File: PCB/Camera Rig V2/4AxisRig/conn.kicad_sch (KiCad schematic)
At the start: 8 parts, among them J5 USB_C_Receptacle_USB2.0_14P

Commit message: PCB V2 first draft
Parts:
- removed J5: USB_C_Receptacle_USB2.0_14P, USB_C_Receptacle_USB2.0_14P:CONN_8p94X6p5X3p16_12L_GCC, symbol Connector:USB_C_Receptacle_USB2.0_14P
- added J5: USB_C_Receptacle_USB2.0_16P, USB_C_Receptacle_USB2.0_14P:CONN_8p94X6p5X3p16_12L_GCC, symbol Connector:USB_C_Receptacle_USB2.0_16P
- R36: renamed from R35; value 5.1k -> 5.1k+-10%
- R37: renamed from R36; value 5.1k -> 5.1k+-10%
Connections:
- net D+: now also J5.A6 (D+), J5.B6 (D+)
- net D-: now also J5.A7 (D-), J5.B7 (D-)
- net GND: now also J5.A1 (GND), J5.A12 (GND), J5.B1 (GND), J5.B12 (GND), J5.S1 (SHIELD)
- net VBUS: now also J5.A4 (VBUS), J5.A9 (VBUS), J5.B4 (VBUS), J5.B9 (VBUS)
- net CC1 renamed USB_CC1
- net USB_CC1: now also J5.A5 (CC1)
- net CC2 renamed USB_CC2
- net USB_CC2: now also J5.B5 (CC2)
- no-connect marks 0 -> 2
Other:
- moved on the sheet: R37

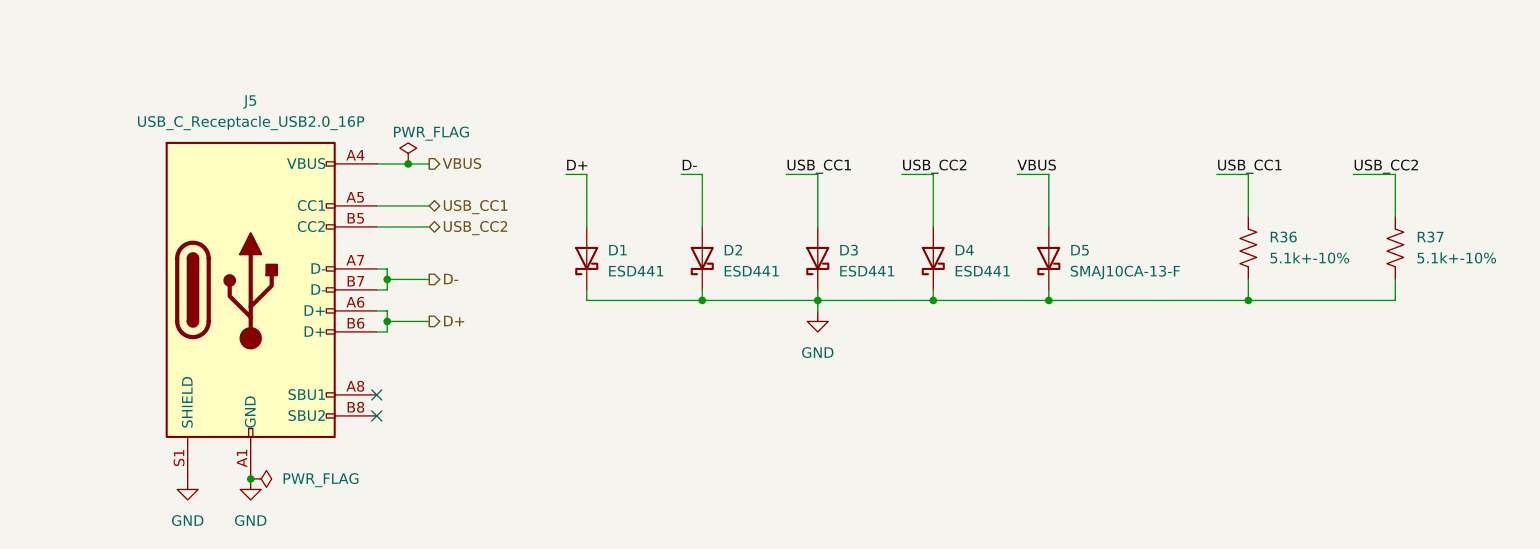
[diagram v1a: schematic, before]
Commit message: Netclass Improvements
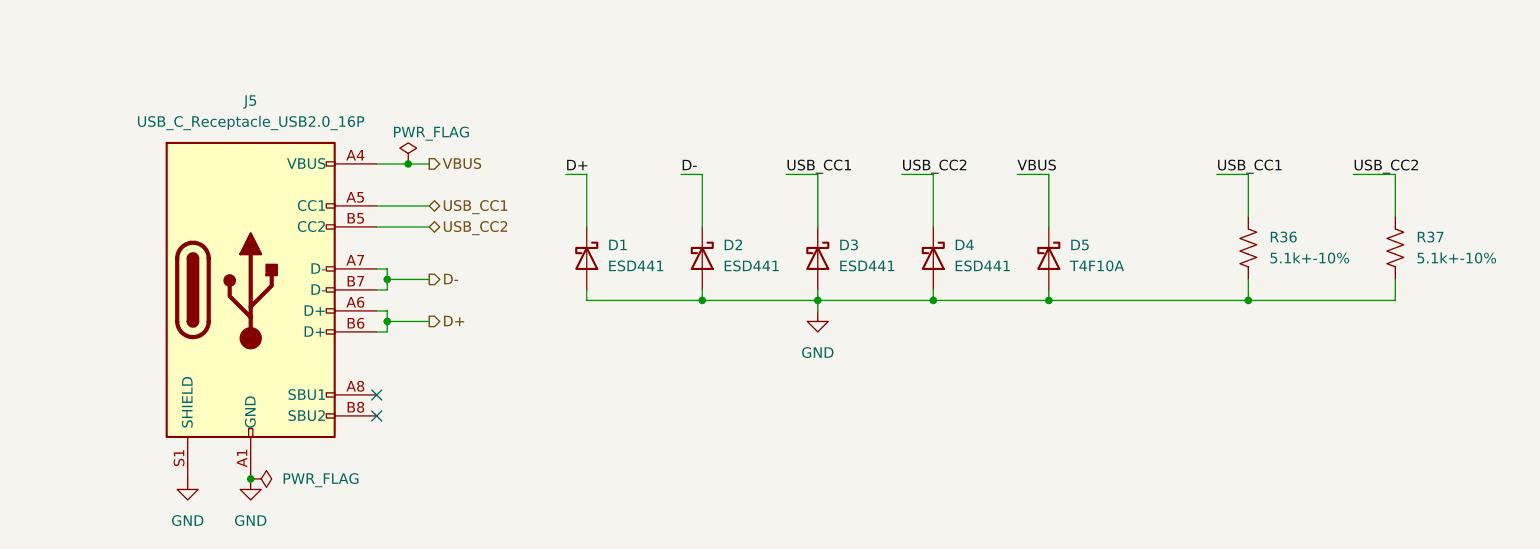
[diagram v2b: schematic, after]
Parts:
- D5: value SMAJ10CA-13-F -> T4F10A; footprint SMAJ10CA-13-F:SMA_DIO -> Diode_SMD:Nexperia_CFP3_SOD-123W
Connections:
- net D+: now also D1.1 (K); no longer D1.2 (A)
- net D-: now also D2.1 (K); no longer D2.2 (A)
- net GND: now also D1.2 (A), D2.2 (A), D3.2 (A), D4.2 (A), D5.2 (A); no longer D1.1 (K), D2.1 (K), D3.1 (K), D4.1 (K), D5.1 (K)
- net USB_CC1: now also D3.1 (K); no longer D3.2 (A)
- net USB_CC2: now also D4.1 (K); no longer D4.2 (A)
- net VBUS: now also D5.1 (K); no longer D5.2 (A)
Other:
- moved on the sheet: D1, D2, D3, D4, D5
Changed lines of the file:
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@@
 	(symbol
 		(lib_id "Device:D_Schottky")
-		(at 146.05 90.17 90)
+		(at 146.05 90.17 270)
 		(unit 1)
 		(exclude_from_sim no)
@@
 		(fields_autoplaced yes)
 		(property "Reference" "D2"
-			(at 148.59 89.2174 90)
-			(effects
-				(font
-					(size 1.27 1.27)
-				)
-				(justify right)
+			(at 148.59 88.5824 90)
+			(effects
+				(font
+					(size 1.27 1.27)
+				)
+				(justify left)
 			)
 		)
 		(property "Value" "ESD441"
-			(at 148.59 91.7574 90)
-			(effects
-				(font
-					(size 1.27 1.27)
-				)
-				(justify right)
+			(at 148.59 91.1224 90)
+			(effects
+				(font
+					(size 1.27 1.27)
+				)
+				(justify left)
 			)
 		)
@@
 	(symbol
 		(lib_id "Device:D_Schottky")
-		(at 173.99 90.17 90)
+		(at 173.99 90.17 270)
 		(unit 1)
 		(exclude_from_sim no)
@@
 		(fields_autoplaced yes)
 		(property "Reference" "D4"
-			(at 176.53 89.2174 90)
-			(effects
-				(font
-					(size 1.27 1.27)
-				)
-				(justify right)
+			(at 176.53 88.5824 90)
+			(effects
+				(font
+					(size 1.27 1.27)
+				)
+				(justify left)
 			)
 		)
 		(property "Value" "ESD441"
-			(at 176.53 91.7574 90)
-			(effects
-				(font
-					(size 1.27 1.27)
-				)
-				(justify right)
+			(at 176.53 91.1224 90)
+			(effects
+				(font
+					(size 1.27 1.27)
+				)
+				(justify left)
 			)
 		)
@@
 	(symbol
 		(lib_id "Device:D_Schottky")
-		(at 187.96 90.17 90)
+		(at 187.96 90.17 270)
 		(unit 1)
 		(exclude_from_sim no)
@@
 		(fields_autoplaced yes)
 		(property "Reference" "D5"
-			(at 190.5 89.2174 90)
-			(effects
-				(font
-					(size 1.27 1.27)
-				)
-				(justify right)
-			)
-		)
-		(property "Value" "SMAJ10CA-13-F"
-			(at 190.5 91.7574 90)
-			(effects
-				(font
-					(size 1.27 1.27)
-				)
-				(justify right)
-			)
-		)
-		(property "Footprint" "SMAJ10CA-13-F:SMA_DIO"
+			(at 190.5 88.5824 90)
+			(effects
+				(font
+					(size 1.27 1.27)
+				)
+				(justify left)
+			)
+		)
+		(property "Value" "T4F10A"
+			(at 190.5 91.1224 90)
+			(effects
+				(font
+					(size 1.27 1.27)
+				)
+				(justify left)
+			)
+		)
+		(property "Footprint" "Diode_SMD:Nexperia_CFP3_SOD-123W"
 			(at 187.96 90.17 0)
 			(effects
@@
 			)
 		)
-		(property "Datasheet" "https://www.diodes.com/assets/Datasheets/SMAJ5.0CA-SMAJ200CA.pdf"
+		(property "Datasheet" "DF2B7AFS"
 			(at 187.96 90.17 0)
 			(effects
@@
 	(symbol
 		(lib_id "Device:D_Schottky")
-		(at 160.02 90.17 90)
+		(at 160.02 90.17 270)
 		(unit 1)
 		(exclude_from_sim no)
@@
 		(fields_autoplaced yes)
 		(property "Reference" "D3"
-			(at 162.56 89.2174 90)
-			(effects
-				(font
-					(size 1.27 1.27)
-				)
-				(justify right)
+			(at 162.56 88.5824 90)
+			(effects
+				(font
+					(size 1.27 1.27)
+				)
+				(justify left)
 			)
 		)
 		(property "Value" "ESD441"
-			(at 162.56 91.7574 90)
-			(effects
-				(font
-					(size 1.27 1.27)
-				)
-				(justify right)
+			(at 162.56 91.1224 90)
+			(effects
+				(font
+					(size 1.27 1.27)
+				)
+				(justify left)
 			)
 		)
@@
 	(symbol
 		(lib_id "Device:D_Schottky")
-		(at 132.08 90.17 90)
+		(at 132.08 90.17 270)
 		(unit 1)
 		(exclude_from_sim no)
@@
 		(fields_autoplaced yes)
 		(property "Reference" "D1"
-			(at 134.62 89.2174 90)
-			(effects
-				(font
-					(size 1.27 1.27)
-				)
-				(justify right)
+			(at 134.62 88.5824 90)
+			(effects
+				(font
+					(size 1.27 1.27)
+				)
+				(justify left)
 			)
 		)
 		(property "Value" "ESD441"
-			(at 134.62 91.7574 90)
-			(effects
-				(font
-					(size 1.27 1.27)
-				)
-				(justify right)
-			)
-		)
+			(at 134.62 91.1224 90)
+			(effects
+				(font
+					(size 1.27 1.27)
+				)
+				(justify left)
+			)
+		)
